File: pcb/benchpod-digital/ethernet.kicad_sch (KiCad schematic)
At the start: 37 parts, among them J7 HR911105A_C12074, U6 LAN8742AI-CZ-TR, Y1 6pF ±10ppm SMD2016-4P Crystal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

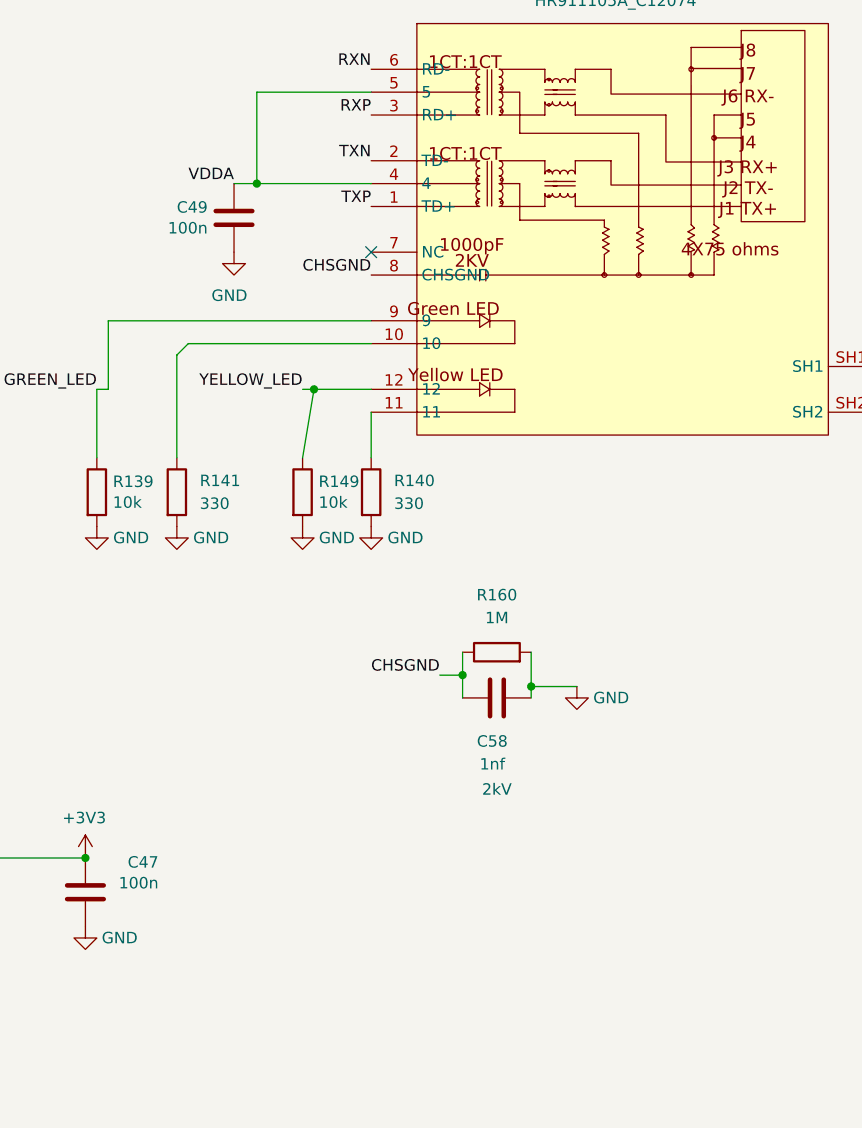
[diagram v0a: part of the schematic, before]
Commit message: digital v3r3: EMC changes from vendor references
Ethernet (Microchip LAN8742A datasheet Fig. 3-23 + EVB8742, HanRun
HR911105A note, TI DP83825 EVM):
- R160 1M -> 0R 0402: J7 pin 8 (CHS GND) straight to GND; C58 DNP
- J7 center taps on their own net ETH_CT, fed from VDDA by R196 0R;
  C49 100n now sits on ETH_CT (place it at J7 pins 4/5)
- C273-C276 8.2p from TXP/TXN/RXP/RXN to GND (EVB8742 10 pF EMI option)

Power terminals (TI TPS25947EVM):
- 100n + 470p at J5 (C277/C278), J6 (C279/C280), J4 (C281/C282)
- J4 pin 1 net named EXT_IN

No new BOM lines. ERC unchanged (467 before and after).

Co-Authored-By: Claude Opus 5.5 <noreply@anthropic.com>
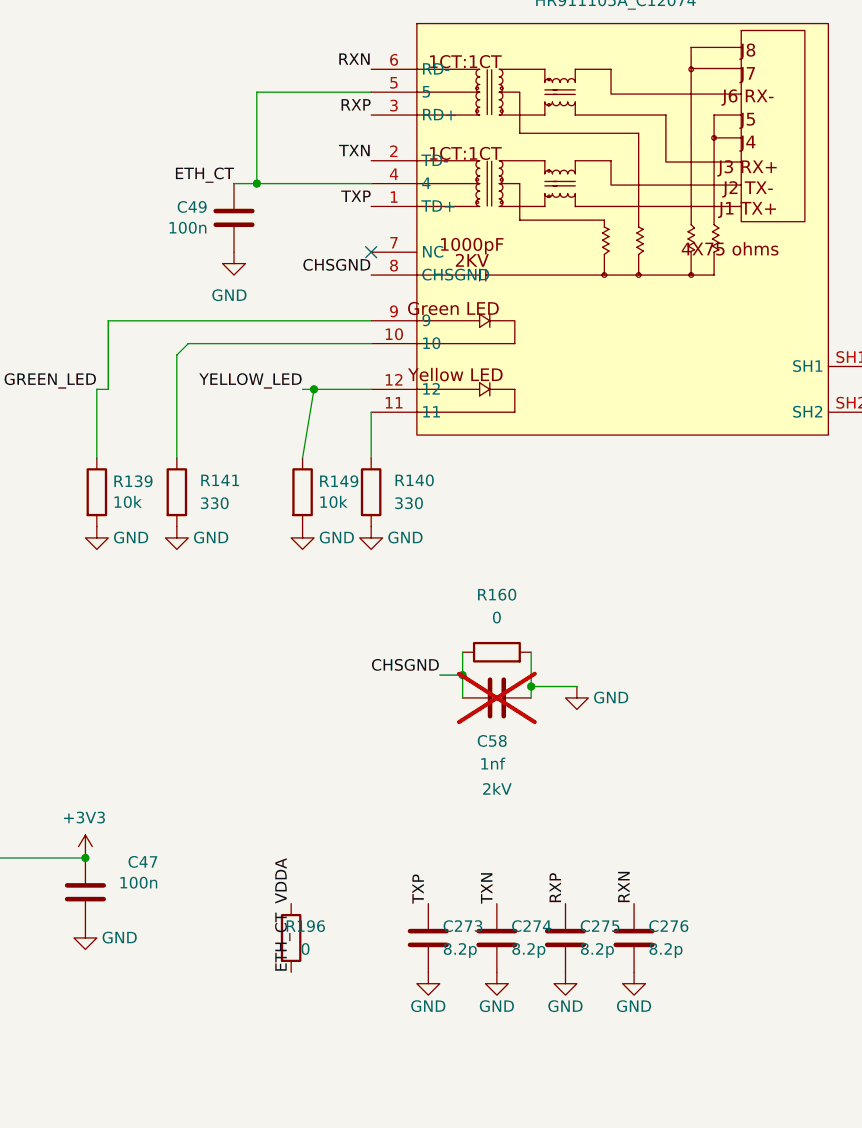
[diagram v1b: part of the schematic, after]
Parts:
- added C273, C274, C275, C276: 8.2p, Capacitor_SMD:C_0402_1005Metric, symbol Device:C
- added R196: 0, Resistor_SMD:R_0402_1005Metric, symbol Device:R
- C58: now not fitted
- R160: value 1M -> 0; footprint Resistor_SMD:R_0603_1608Metric -> Resistor_SMD:R_0402_1005Metric; LCSC C22935 -> C17168
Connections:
- net GND: now also C273.2, C274.2, C275.2, C276.2
- net RXN: now also C276.1
- net RXP: now also C275.1
- net TXN: now also C274.1
- net TXP: now also C273.1
- net VDDA: now also R196.1; no longer C49.1, J7.4, J7.5
- new net ETH_CT: C49.1, J7.4, J7.5, R196.2
